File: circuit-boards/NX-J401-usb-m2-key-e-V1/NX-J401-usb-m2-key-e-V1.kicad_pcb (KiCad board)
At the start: 2 copper layers, 30 x 22 mm, 3 parts, among them J1 USB1, J2 Bus_M.2_Socket_E

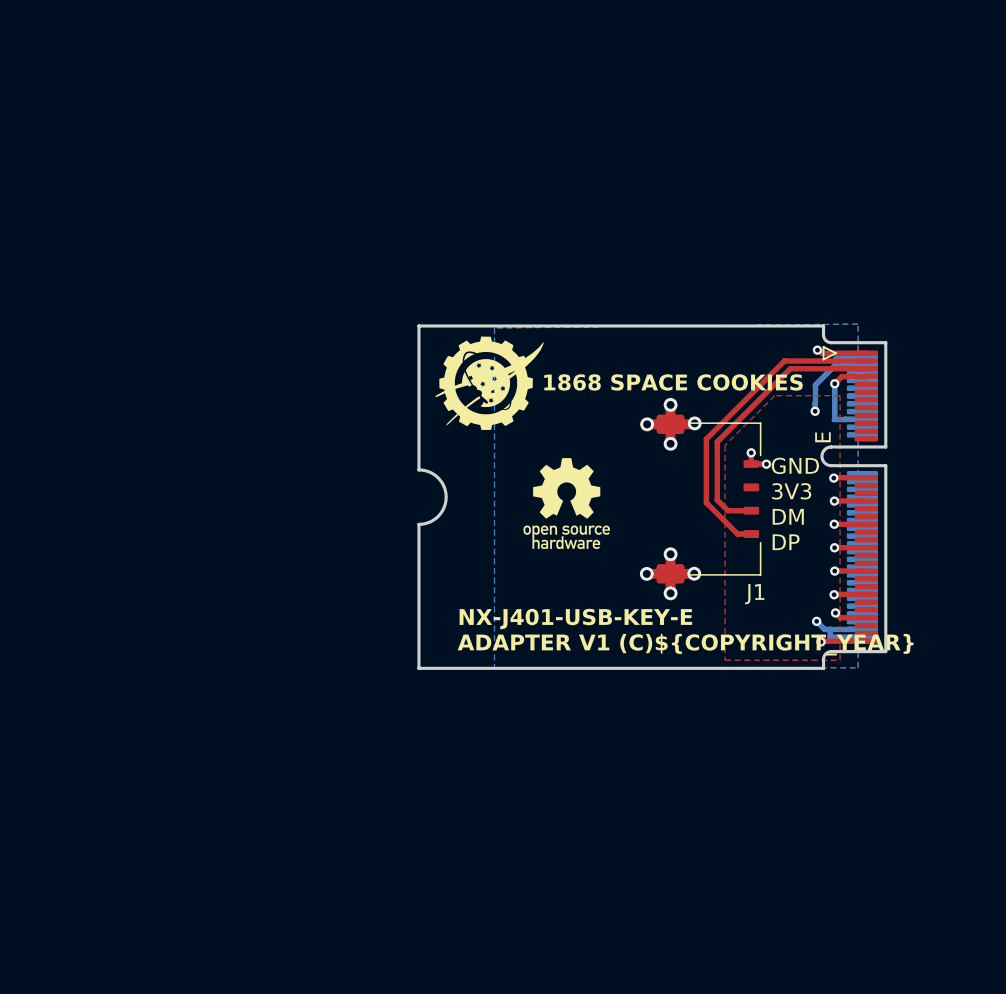
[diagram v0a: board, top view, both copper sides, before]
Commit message: Add rails to M.2 adapter.  Minor fixes to NX J401 adapter
Signed-off-by: Scott Berman <sgberman1@gmail.com>
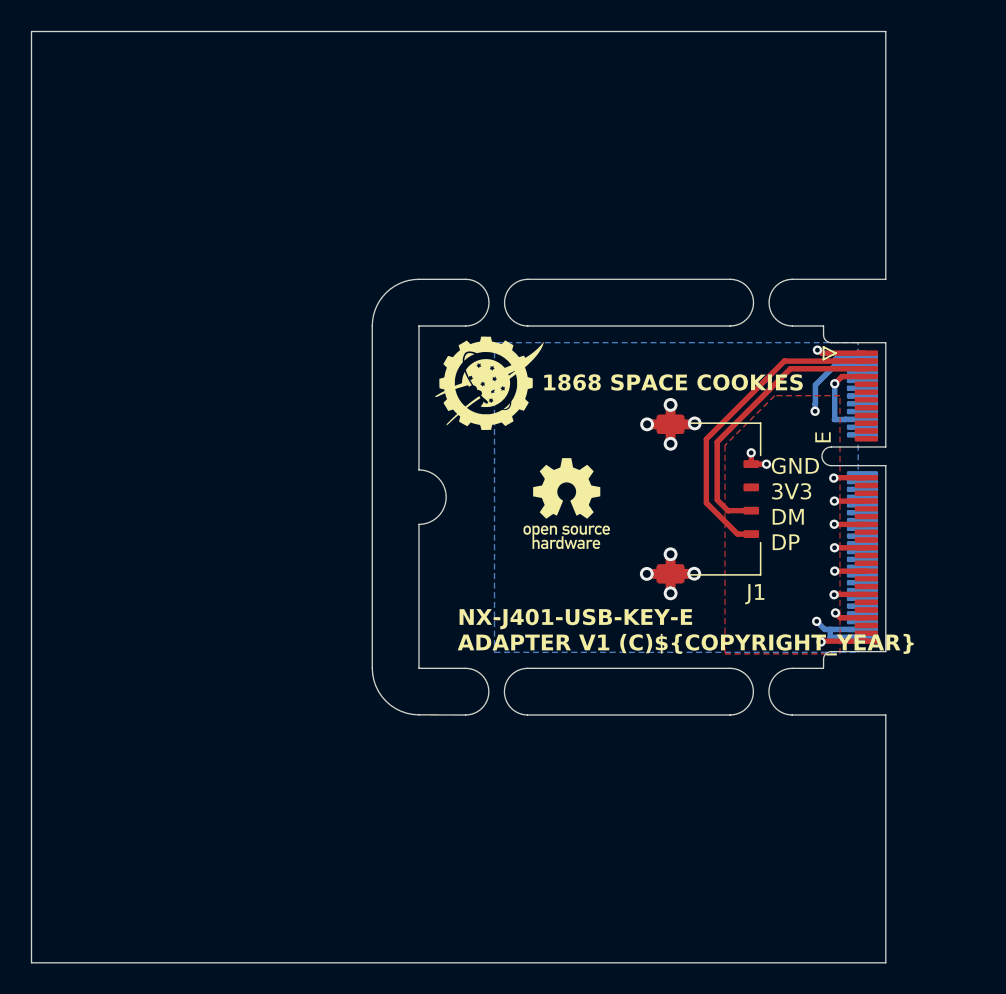
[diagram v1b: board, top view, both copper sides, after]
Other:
- board size 30 x 22 mm -> 54.9 x 59.8 mm

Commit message: Prepare USB-m2 for manufacture
Signed-off-by: Scott Berman <sgberman1@gmail.com>
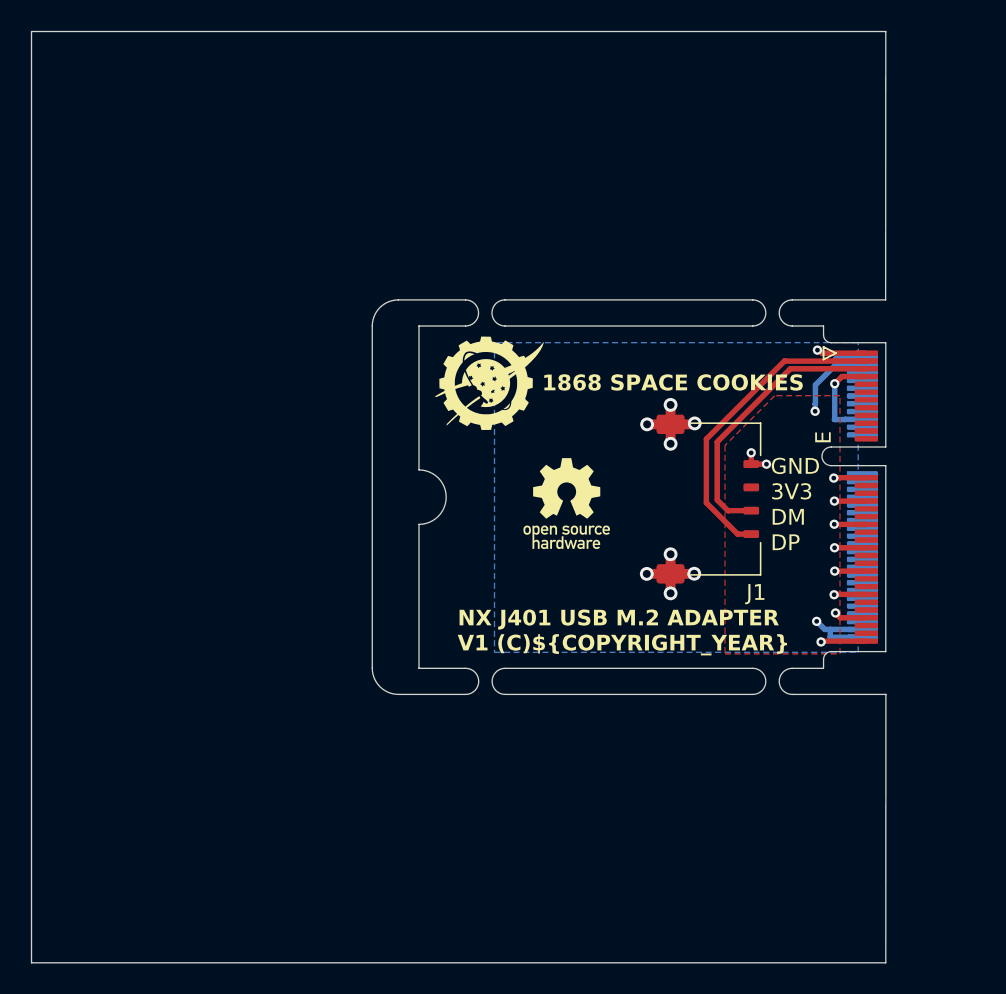
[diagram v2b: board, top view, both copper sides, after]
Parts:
- J1: footprint usb-m2-key-e-adapter:Molex-PicoLatch-5040500491 -> nx-j401-usb-m2-key-e:Molex-PicoLatch-5040500491
- J2: footprint Connector_PCBEdge:M.2_2230-xx-E -> nx-j401-usb-m2-key-e:M.2_2230-xx-E
- LOGO1: footprint usb-m2-key-e-adapter:SPACE_COOKIES_LOGO_7mm -> nx-j401-usb-m2-key-e:SPACE_COOKIES_LOGO_7mm
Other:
- outline, holes or cut-outs redrawn
- board text added: "${COMPANY}"
- board text added: "${TITLE} V${REVISION} (C)${COPYRIGHT_YEAR}"
- board text added: "FRONT"
- board text removed: "1868 SPACE COOKIES"
- board text removed: "NX-J401-USB-KEY-E ADAPTER V1 (C)${COPYRIGHT_YEAR}"
